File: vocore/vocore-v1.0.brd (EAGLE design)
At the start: 25.6 x 25.6 mm, 146 parts, among them CON2 5020, U1 TFBGA196, U25 U4, U3 SO8, U33 Y1, U35 TSOP2-54P-400MIL, U8 LDO1, U9 LDO1

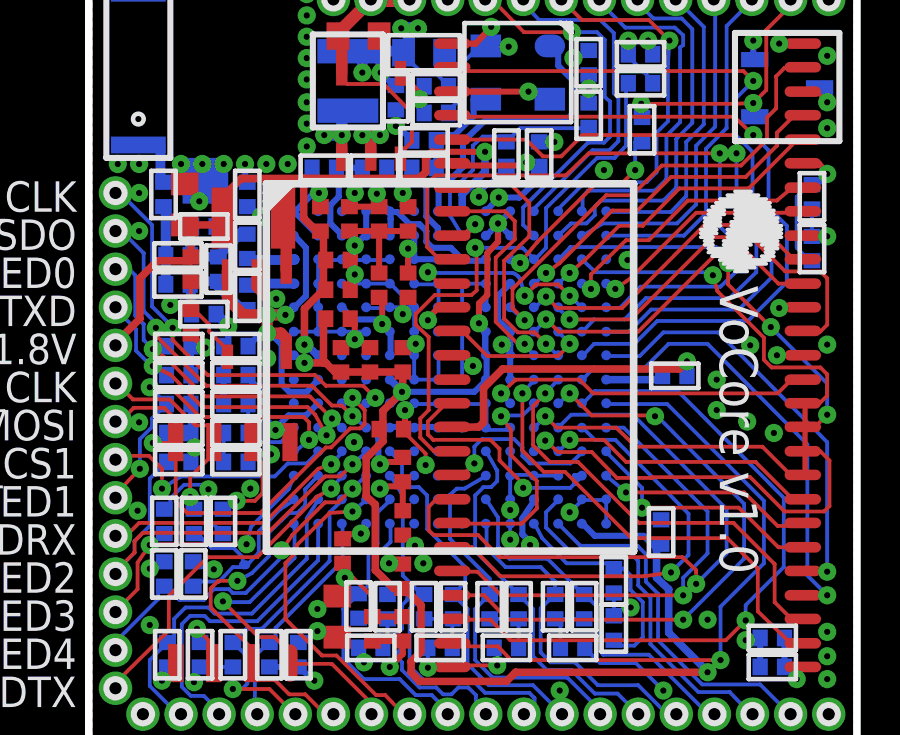
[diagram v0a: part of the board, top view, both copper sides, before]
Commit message: adding lbr.
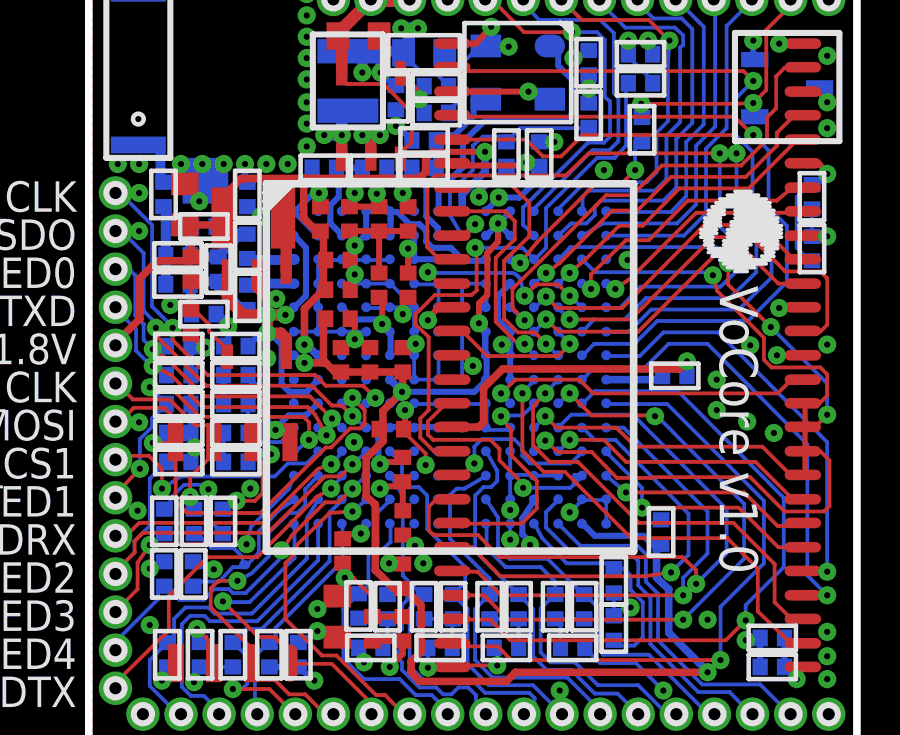
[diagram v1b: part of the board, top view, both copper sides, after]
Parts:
- CON2: device VoCore.v1.0:5020_1PRIMARY -> vocore-v1.0:5020_1PRIMARY
- L15: device VoCore.v1.0:0806_1PRIMARY -> vocore-v1.0:0806_1PRIMARY
- U1: device VoCore.v1.0:TFBGA196_1PRIMARY -> vocore-v1.0:TFBGA196_1PRIMARY
- U25: device VoCore.v1.0:U4_1PRIMARY -> vocore-v1.0:U4_1PRIMARY
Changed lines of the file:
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@@
 <grid distance="0.05" unitdist="inch" unit="inch" style="lines" multiple="1" display="yes" altdistance="0.005" altunitdist="inch" altunit="inch"/>
 <layers>
-<layer number="1" name="Top" color="4" fill="1" visible="no" active="yes"/>
+<layer number="1" name="Top" color="4" fill="1" visible="yes" active="yes"/>
 <layer number="2" name="Route2" color="1" fill="3" visible="no" active="yes"/>
 <layer number="3" name="Route3" color="4" fill="3" visible="no" active="yes"/>
@@
 <layer number="14" name="Route14" color="1" fill="6" visible="no" active="no"/>
 <layer number="15" name="Route15" color="4" fill="6" visible="no" active="no"/>
-<layer number="16" name="Bottom" color="1" fill="1" visible="no" active="yes"/>
-<layer number="17" name="Pads" color="2" fill="1" visible="no" active="yes"/>
-<layer number="18" name="Vias" color="2" fill="1" visible="no" active="yes"/>
+<layer number="16" name="Bottom" color="1" fill="1" visible="yes" active="yes"/>
+<layer number="17" name="Pads" color="2" fill="1" visible="yes" active="yes"/>
+<layer number="18" name="Vias" color="2" fill="1" visible="yes" active="yes"/>
 <layer number="19" name="Unrouted" color="6" fill="1" visible="yes" active="yes"/>
-<layer number="20" name="Dimension" color="15" fill="1" visible="no" active="yes"/>
-<layer number="21" name="tPlace" color="7" fill="1" visible="no" active="yes"/>
-<layer number="22" name="bPlace" color="7" fill="1" visible="no" active="yes"/>
-<layer number="23" name="tOrigins" color="15" fill="1" visible="no" active="yes"/>
-<layer number="24" name="bOrigins" color="15" fill="1" visible="no" active="yes"/>
+<layer number="20" name="Dimension" color="15" fill="1" visible="yes" active="yes"/>
+<layer number="21" name="tPlace" color="7" fill="1" visible="yes" active="yes"/>
+<layer number="22" name="bPlace" color="7" fill="1" visible="yes" active="yes"/>
+<layer number="23" name="tOrigins" color="15" fill="1" visible="yes" active="yes"/>
+<layer number="24" name="bOrigins" color="15" fill="1" visible="yes" active="yes"/>
 <layer number="25" name="tNames" color="7" fill="1" visible="no" active="yes"/>
 <layer number="26" name="bNames" color="7" fill="1" visible="no" active="yes"/>
@@
 <layer number="43" name="vRestrict" color="2" fill="10" visible="no" active="yes"/>
 <layer number="44" name="Drills" color="7" fill="1" visible="no" active="yes"/>
-<layer number="45" name="Holes" color="7" fill="1" visible="no" active="yes"/>
+<layer number="45" name="Holes" color="7" fill="1" visible="yes" active="yes"/>
 <layer number="46" name="Milling" color="3" fill="1" visible="no" active="yes"/>
 <layer number="47" name="Measures" color="7" fill="1" visible="no" active="yes"/>
 <layer number="48" name="Document" color="7" fill="1" visible="no" active="yes"/>
 <layer number="49" name="Reference" color="7" fill="1" visible="no" active="yes"/>
-<layer number="51" name="tDocu" color="7" fill="1" visible="no" active="yes"/>
+<layer number="51" name="tDocu" color="7" fill="1" visible="yes" active="yes"/>
 <layer number="52" name="bDocu" color="7" fill="1" visible="no" active="yes"/>
 <layer number="90" name="Modules" color="5" fill="1" visible="no" active="no"/>
@@
 <attribute name="VALUE" x="262.3566" y="265.811" size="2.032" layer="28" font="vector" ratio="13" rot="SMR180" display="off"/>
 </element>
-<element name="CON2" library="VoCore.v1.0" package="5020_1PRIMARY" value="5020" x="254.0508" y="277.0886" smashed="yes" rot="R270">
+<element name="CON2" library="vocore-v1.0" package="5020_1PRIMARY" value="5020" x="254.0508" y="277.0886" smashed="yes" rot="R270">
 <attribute name="NAME" x="254.0508" y="277.0886" size="2.032" layer="25" font="vector" ratio="13" rot="SR270" display="off"/>
 <attribute name="VALUE" x="254.0508" y="277.0886" size="2.032" layer="27" font="vector" ratio="13" rot="SR270" display="off"/>
@@
 <attribute name="VALUE" x="258.4704" y="270.5862" size="2.032" layer="28" font="vector" ratio="13" rot="SMR0" display="off"/>
 </element>
-<element name="L15" library="VoCore.v1.0" package="0806_1PRIMARY" value="0806" x="261.5692" y="275.1074" smashed="yes" rot="R90">
+<element name="L15" library="vocore-v1.0" package="0806_1PRIMARY" value="0806" x="261.5692" y="275.1074" smashed="yes" rot="R90">
 <attribute name="NAME" x="261.5692" y="275.1074" size="2.032" layer="25" font="vector" ratio="13" rot="SR90" display="off"/>
 <attribute name="VALUE" x="261.5692" y="275.1074" size="2.032" layer="27" font="vector" ratio="13" rot="SR90" display="off"/>
@@
 <attribute name="VALUE" x="256.9464" y="273.05" size="2.032" layer="27" font="vector" ratio="13" rot="SR0" display="off"/>
 </element>
-<element name="U1" library="VoCore.v1.0" package="TFBGA196_1PRIMARY" value="TFBGA196" x="265.0236" y="265.557" smashed="yes">
+<element name="U1" library="vocore-v1.0" package="TFBGA196_1PRIMARY" value="TFBGA196" x="265.0236" y="265.557" smashed="yes">
 <attribute name="NAME" x="265.0236" y="265.557" size="2.032" layer="25" font="vector" ratio="13" rot="SR0" display="off"/>
 <attribute name="VALUE" x="265.0236" y="265.557" size="2.032" layer="27" font="vector" ratio="13" rot="SR0" display="off"/>
 </element>
-<element name="U25" library="VoCore.v1.0" package="U4_1PRIMARY" value="U4" x="275.1836" y="273.9136" smashed="yes" rot="R180">
+<element name="U25" library="vocore-v1.0" package="U4_1PRIMARY" value="U4" x="275.1836" y="273.9136" smashed="yes" rot="R180">
 <attribute name="NAME" x="275.1836" y="273.9136" size="2.032" layer="25" font="vector" ratio="13" rot="SR180" display="off"/>
 <attribute name="VALUE" x="275.1836" y="273.9136" size="2.032" layer="27" font="vector" ratio="13" rot="SR180" display="off"/>
